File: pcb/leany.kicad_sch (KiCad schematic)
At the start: 37 parts, among them J1 ST7735S, J2 SWD, Q1 AO3401A, SW1 ZERO, SW2 HOLD, SW3 RESET, SW4 FLASH, U1 STM32F103C8Tx, U3 BMI270, U6 CH340N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

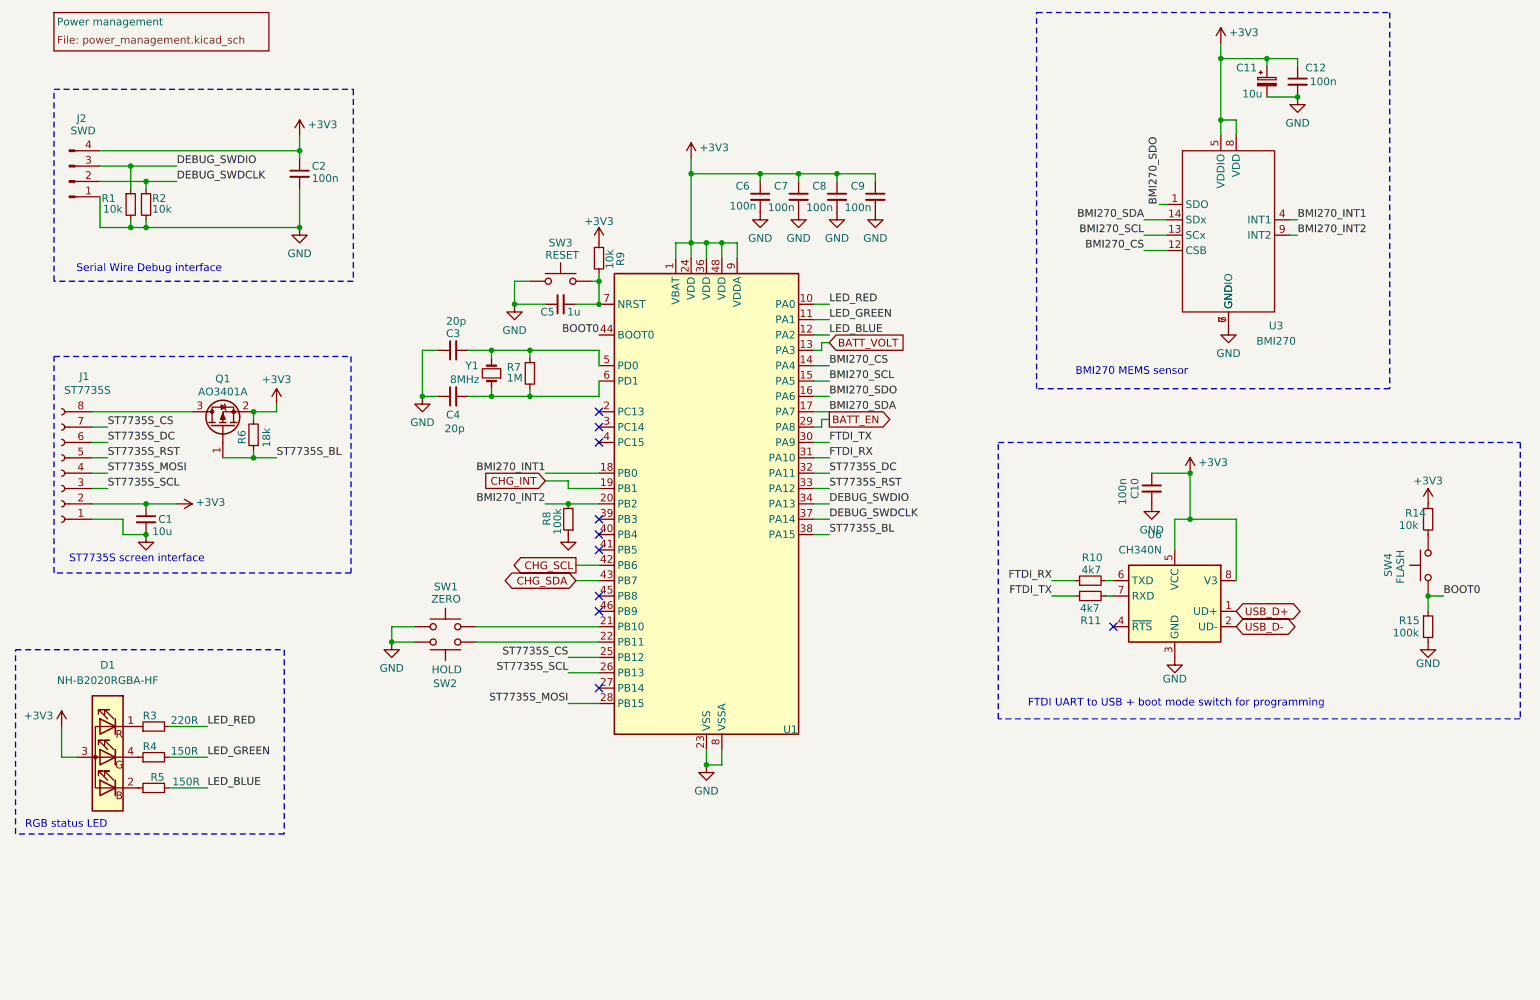
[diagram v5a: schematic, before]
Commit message: add pull-up resistors to CS pins
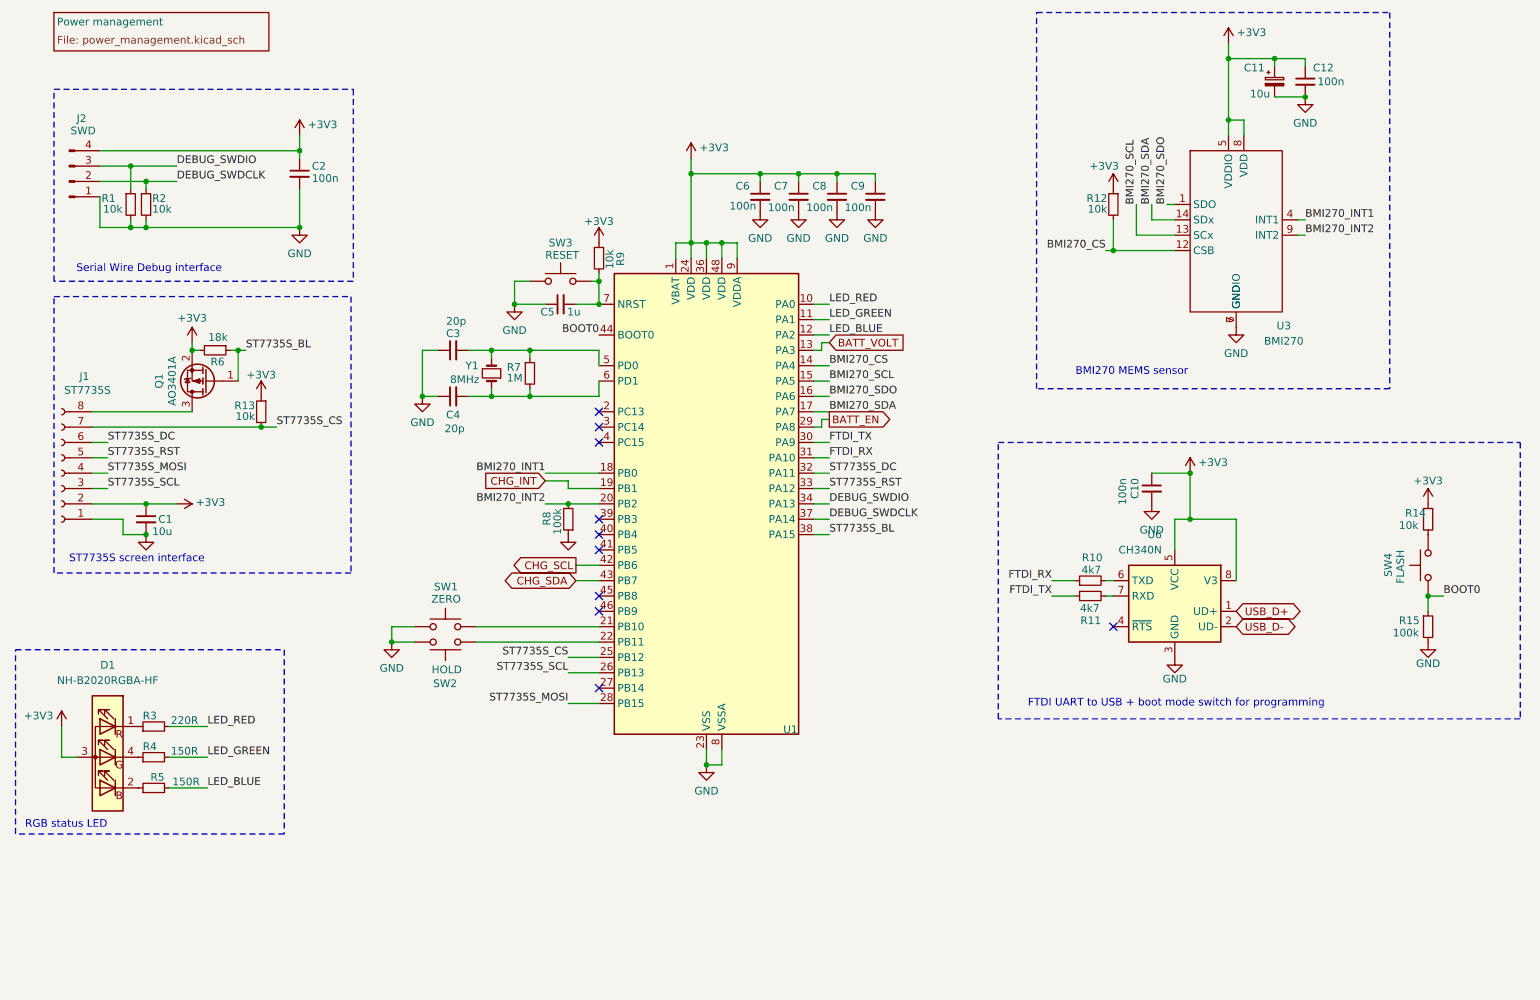
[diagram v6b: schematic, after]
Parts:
- added R12, R13: 10k, Resistor_SMD:R_0603_1608Metric, symbol Device:R_Small
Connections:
- net +3V3: now also R12.1, R13.1
- net BMI270_CS: now also R12.2
- net ST7735S_CS: now also R13.2
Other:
- moved on the sheet: C11, C12, Q1, R6, U3

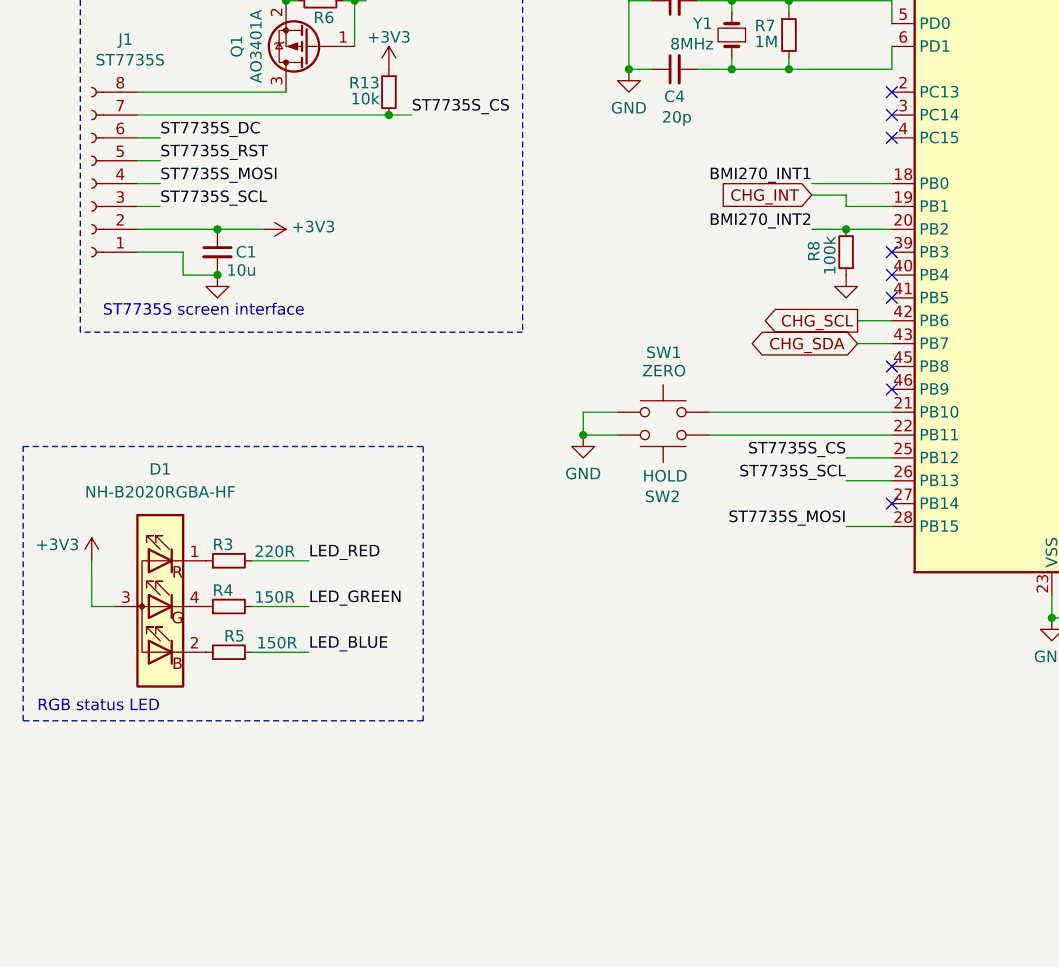
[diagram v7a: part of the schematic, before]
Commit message: add a debug pad
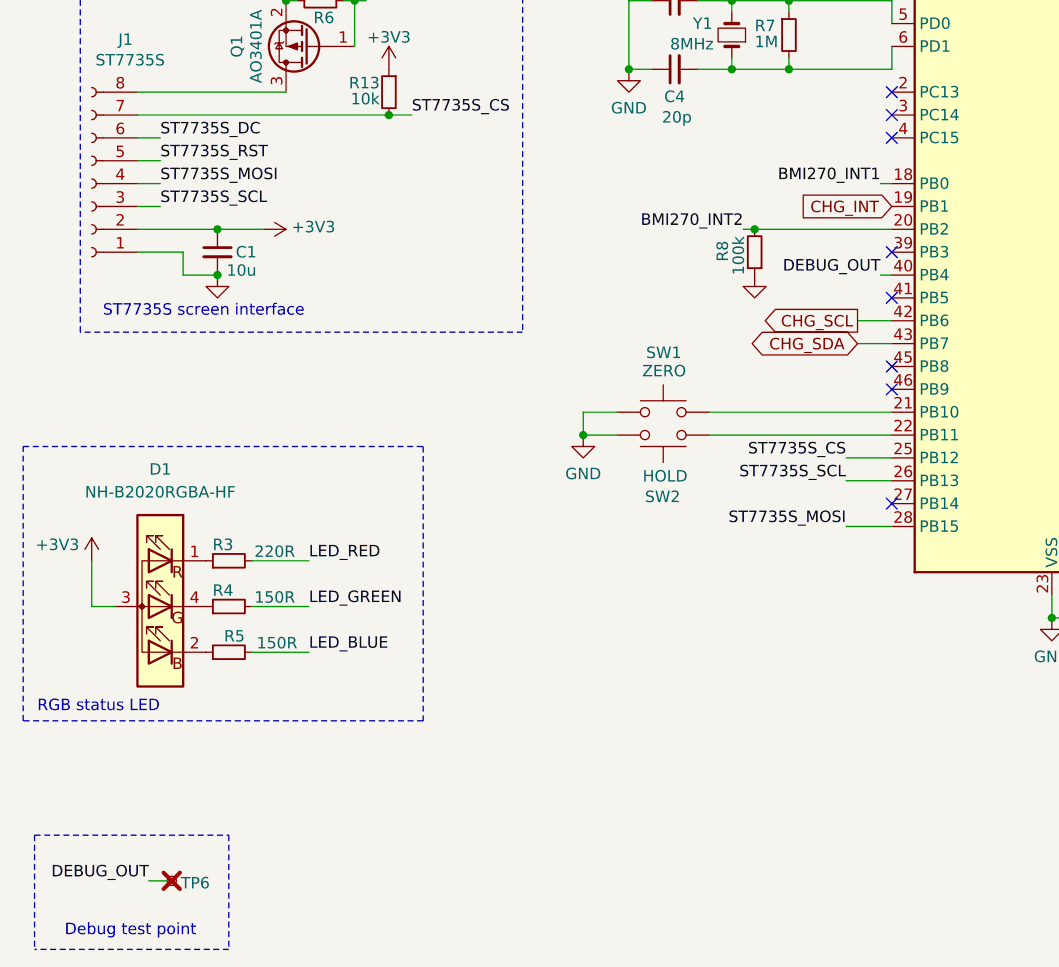
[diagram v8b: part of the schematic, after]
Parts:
- added TP6: DEBUG_OUT, leany_footprints:TestPoint_Pad_1.0x1.0mm, symbol Connector:TestPoint_Small
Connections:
- net DEBUG_OUT: now reaches U1.40 (PB4)
- net DEBUG_OUT: now also TP6.1
- no-connect marks 10 -> 9
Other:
- note added: "Debug test point"
- moved on the sheet: R8
